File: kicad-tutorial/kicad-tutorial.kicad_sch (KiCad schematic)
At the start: 3 parts

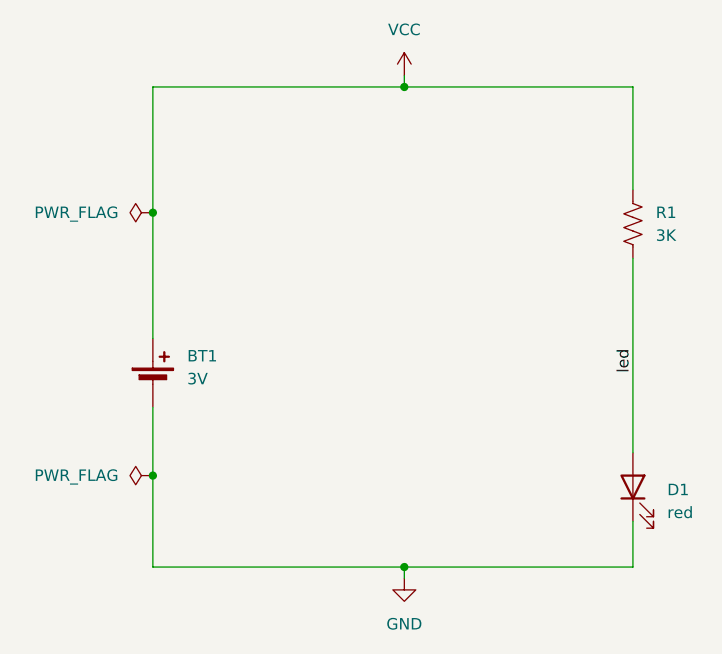
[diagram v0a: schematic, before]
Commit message: add switch to kicad-tutorial
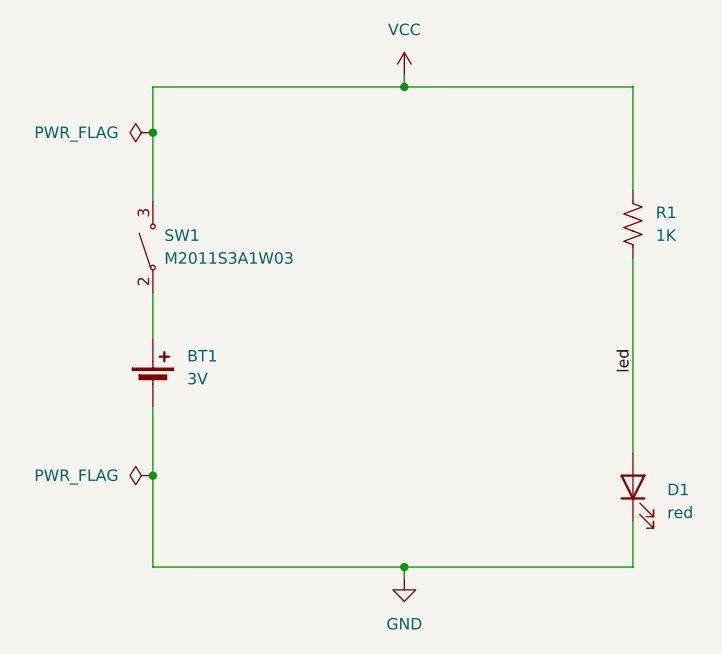
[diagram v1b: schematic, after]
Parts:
- added SW1: M2011S3A1W03, getting-started:Switch_Toggle_SPST_NKK_M2011S3A1x03, symbol getting-started:M2011S3A1W03
- R1: value 3K -> 1K
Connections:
- net VCC: now also SW1.3 (A); no longer BT1.1 (+)
- new net: BT1.1 (+), SW1.2 (A)
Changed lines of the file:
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@@
-	)
-	(junction
-		(at 106.68 62.23)
-		(diameter 0)
-		(color 0 0 0 0)
 	)
 	(junction
@@
 		(color 0 0 0 0)
 	)
+	(junction
+		(at 106.68 53.34)
+		(diameter 0)
+		(color 0 0 0 0)
+	)
 	(wire
 		(pts
@@
 	(wire
 		(pts
-			(xy 106.68 62.23) (xy 106.68 48.26)
-		)
-		(stroke
-			(width 0)
-			(type default)
-		)
-	)
-	(wire
-		(pts
 			(xy 134.62 101.6) (xy 106.68 101.6)
 		)
@@
 	(wire
 		(pts
+			(xy 106.68 48.26) (xy 106.68 53.34)
+		)
+		(stroke
+			(width 0)
+			(type default)
+		)
+	)
+	(wire
+		(pts
 			(xy 160.02 101.6) (xy 134.62 101.6)
 		)
@@
 	(wire
 		(pts
-			(xy 106.68 76.2) (xy 106.68 62.23)
+			(xy 106.68 71.12) (xy 106.68 76.2)
 		)
 		(stroke
@@
 		(pts
 			(xy 160.02 48.26) (xy 160.02 59.69)
+		)
+		(stroke
+			(width 0)
+			(type default)
+		)
+	)
+	(wire
+		(pts
+			(xy 106.68 53.34) (xy 106.68 60.96)
 		)
 		(stroke
@@
 	)
 	(symbol
+		(lib_id "getting-started:M2011S3A1W03")
+		(at 106.68 66.04 90)
+		(unit 1)
+		(exclude_from_sim no)
+		(in_bom yes)
+		(on_board yes)
+		(dnp no)
+		(fields_autoplaced yes)
+		(property "Reference" "SW1"
+			(at 107.95 64.7699 90)
+			(effects
+				(font
+					(size 1.27 1.27)
+				)
+				(justify right)
+			)
+		)
+		(property "Value" "M2011S3A1W03"
+			(at 107.95 67.3099 90)
+			(effects
+				(font
+					(size 1.27 1.27)
+				)
+				(justify right)
+			)
+		)
+		(property "Footprint" "getting-started:Switch_Toggle_SPST_NKK_M2011S3A1x03"
+			(at 104.648 67.056 0)
+			(effects
+				(font
+					(size 1.27 1.27)
+				)
+				(hide yes)
+			)
+		)
+		(property "Datasheet" ""
+			(at 104.648 67.056 0)
+			(effects
+				(font
+					(size 1.27 1.27)
+				)
+				(hide yes)
+			)
+		)
+		(property "Description" ""
+			(at 104.648 67.056 0)
+			(effects
+				(font
+					(size 1.27 1.27)
+				)
+				(hide yes)
+			)
+		)
+		(pin "3"
+		)
+		(pin "2"
+		)
+		(instances
+			(project ""
+				(path "/79fea610-35cf-4c04-8af8-948f9b02c242"
+					(reference "SW1")
+					(unit 1)
+				)
+			)
+		)
+	)
+	(symbol
 		(lib_id "Device:Battery_Cell")
 		(at 106.68 81.28 0)
@@
 			)
 		)
-		(property "Value" "3K"
+		(property "Value" "1K"
 			(at 162.56 64.7699 0)
 			(effects
@@
 	(symbol
 		(lib_id "power:PWR_FLAG")
-		(at 106.68 62.23 90)
+		(at 106.68 53.34 90)
 		(unit 1)
 		(exclude_from_sim no)
@@
 		(fields_autoplaced yes)
 		(property "Reference" "#FLG01"
-			(at 104.775 62.23 0)
+			(at 104.775 53.34 0)
 			(effects
 				(font
@@
 		)
 		(property "Value" "PWR_FLAG"
-			(at 102.87 62.2299 90)
+			(at 102.87 53.3399 90)
 			(effects
 				(font
@@
 		)
 		(property "Footprint" ""
-			(at 106.68 62.23 0)
+			(at 106.68 53.34 0)
 			(effects
 				(font
@@
 		)
 		(property "Datasheet" "~"
-			(at 106.68 62.23 0)
+			(at 106.68 53.34 0)
 			(effects
 				(font
@@
 		)
 		(property "Description" "Special symbol for telling ERC where power comes from"
-			(at 106.68 62.23 0)
-			(effects
-				(font
+			(at 106.68 53.34 0)
+			(effects
+				(font
